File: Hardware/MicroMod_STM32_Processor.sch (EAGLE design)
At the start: 36 parts, among them J1 MICROMOD-2222, Q1 MOSFET_PCH-DMG2305UX-7, U1 STM32F405RGT6, U3 W25QXX128MBIT-6X5, Y1 12MHz, Y2 32.768kHz

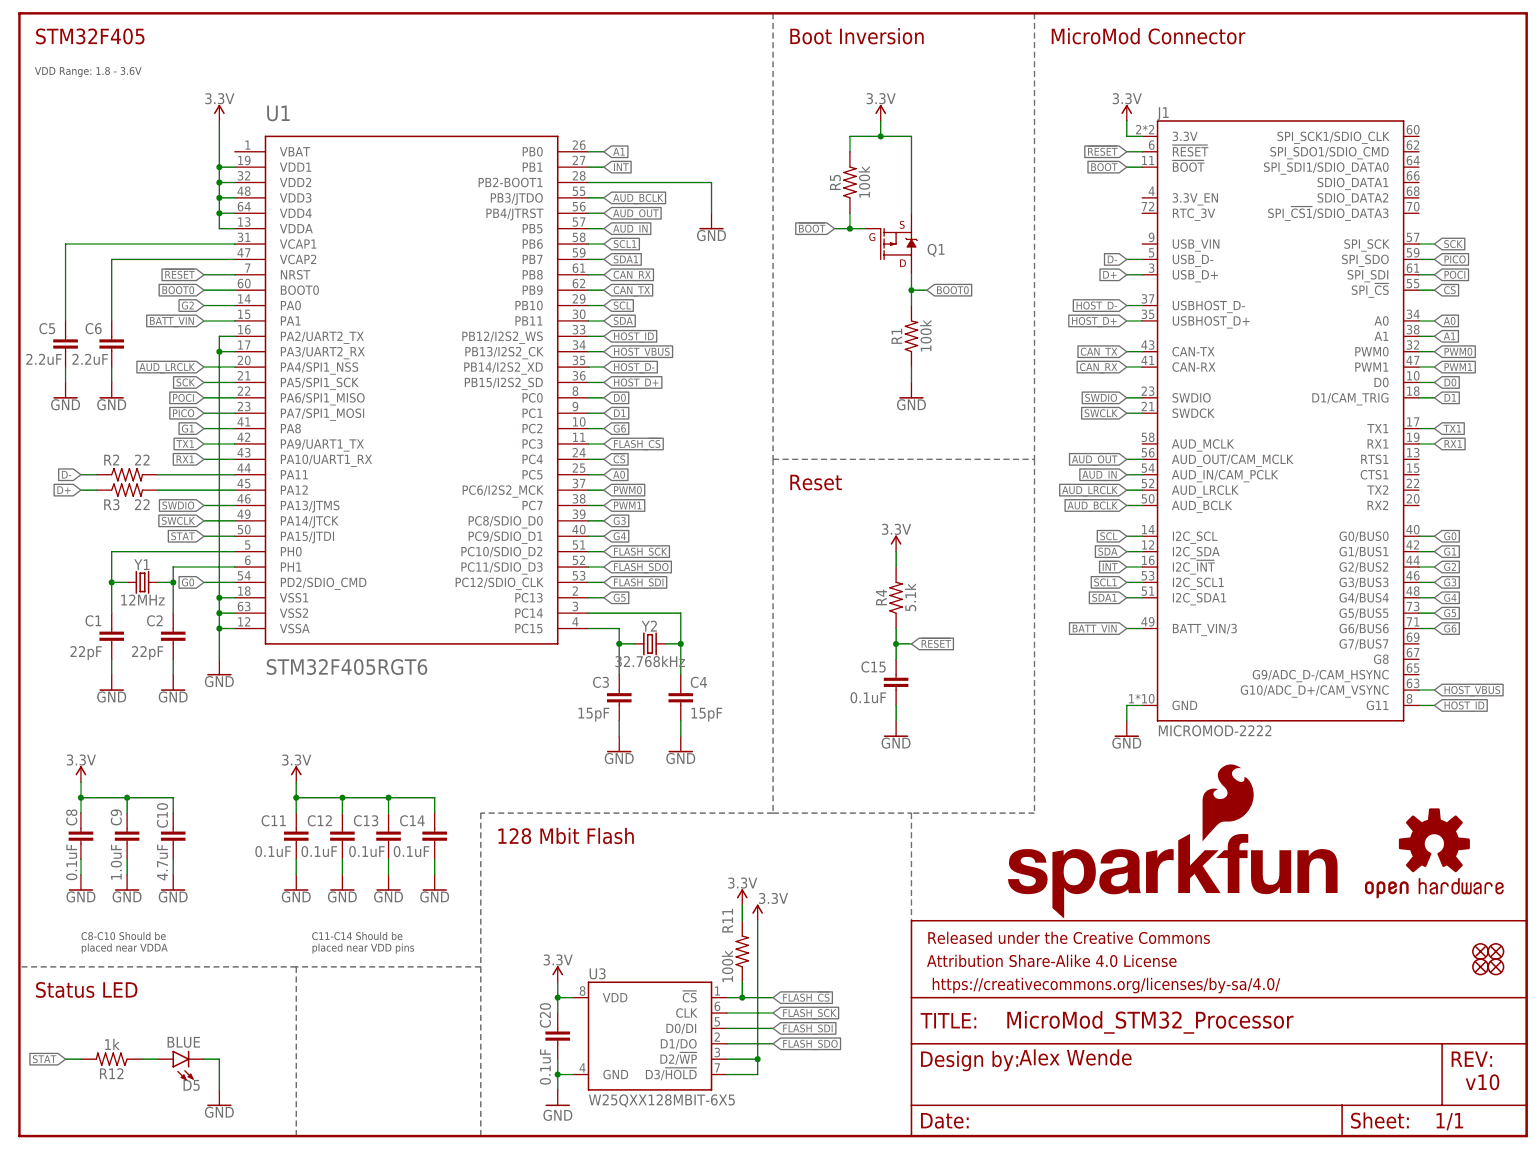
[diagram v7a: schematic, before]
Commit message: Rerouted board, cleaned up schematic.
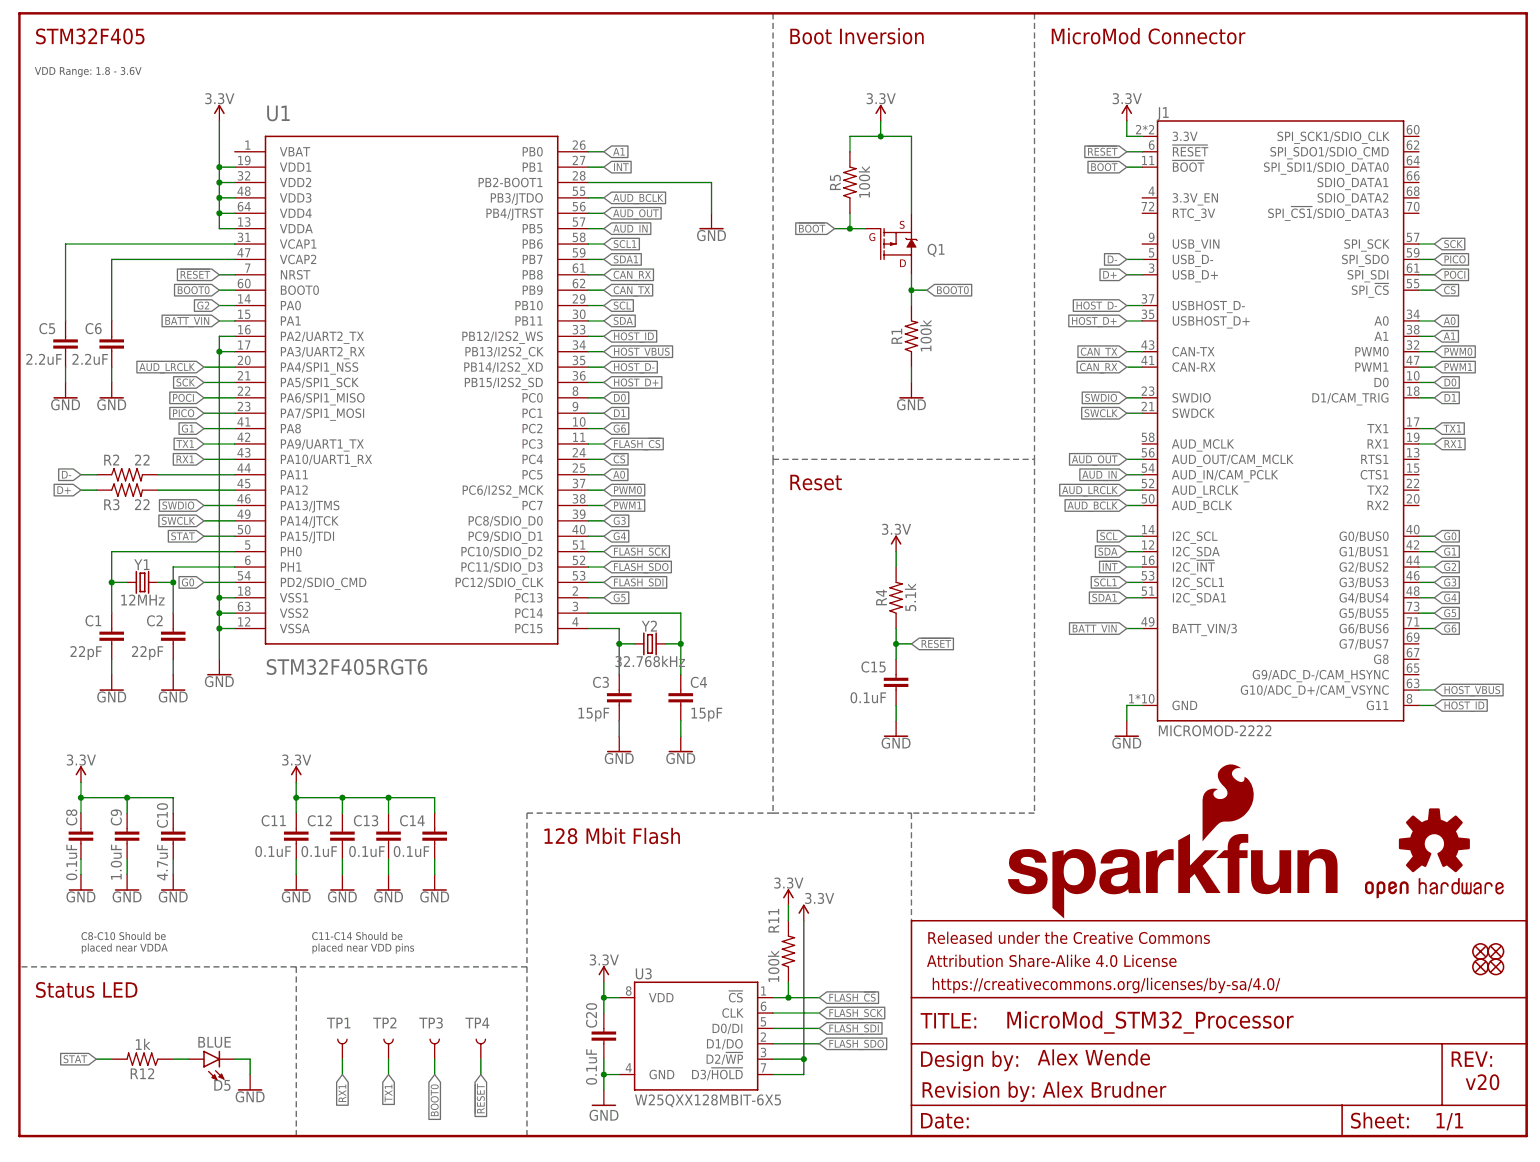
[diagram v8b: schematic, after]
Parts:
- added TP1, TP2, TP3, TP4: TEST-POINTTP_15TH_THRU, SparkFun-Connectors:TEST-POINTTP_15TH_THRU
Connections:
- net !RESET: now also TP4.1
- net BOOT0: now also TP3.1
- net RX1: now also TP1.1
- net TX1: now also TP2.1
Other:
- note added: "Revision by: Alex Brudner"
- note added: "v20"
- note removed: "v10"
- moved on the sheet: C20, D5, R11, R12, U3
